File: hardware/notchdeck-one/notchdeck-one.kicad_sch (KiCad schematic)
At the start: 0 parts

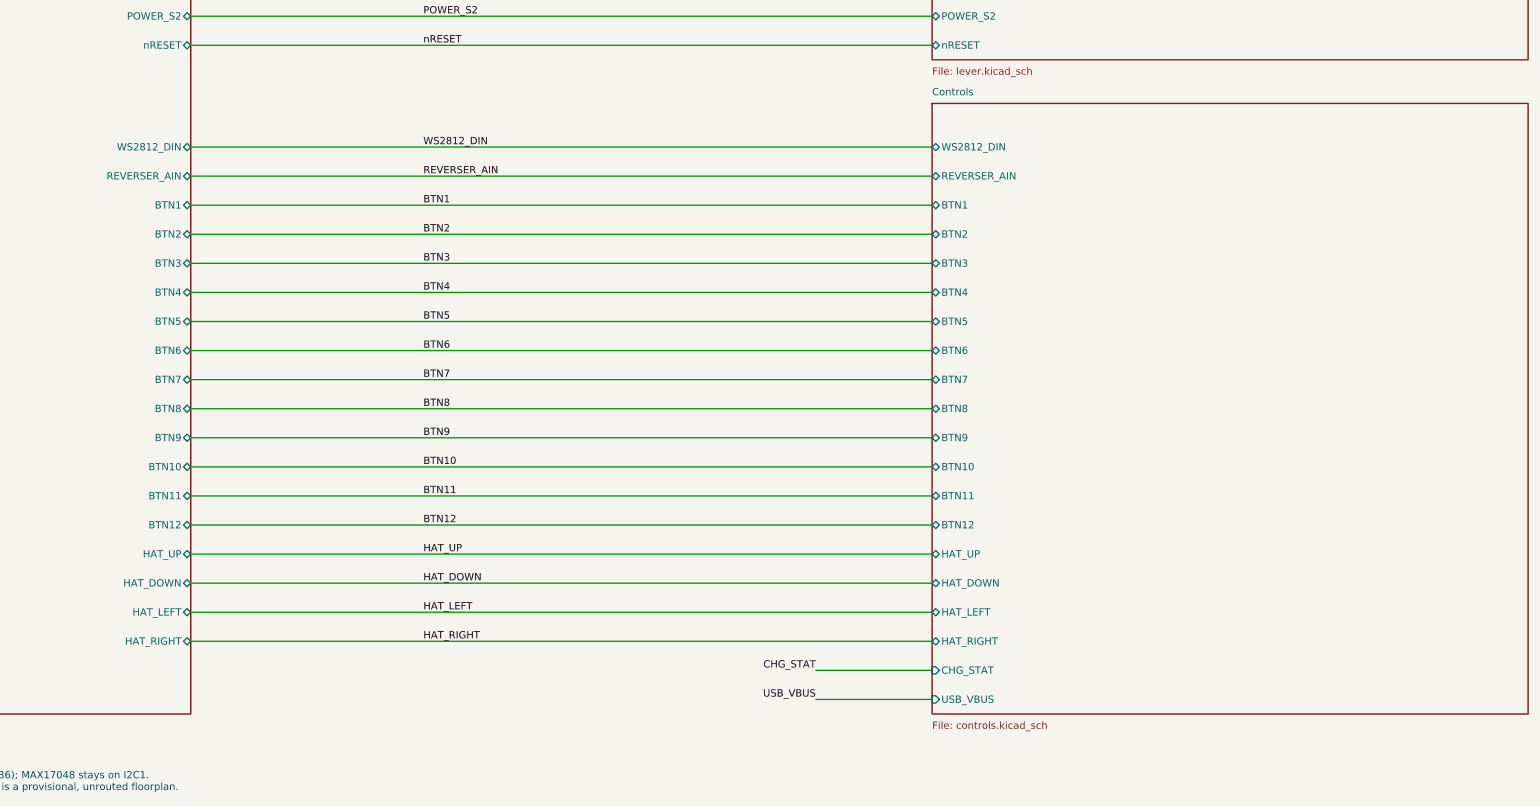
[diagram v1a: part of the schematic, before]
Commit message: Split controller buttons onto stocked STM32G030 panel PCB
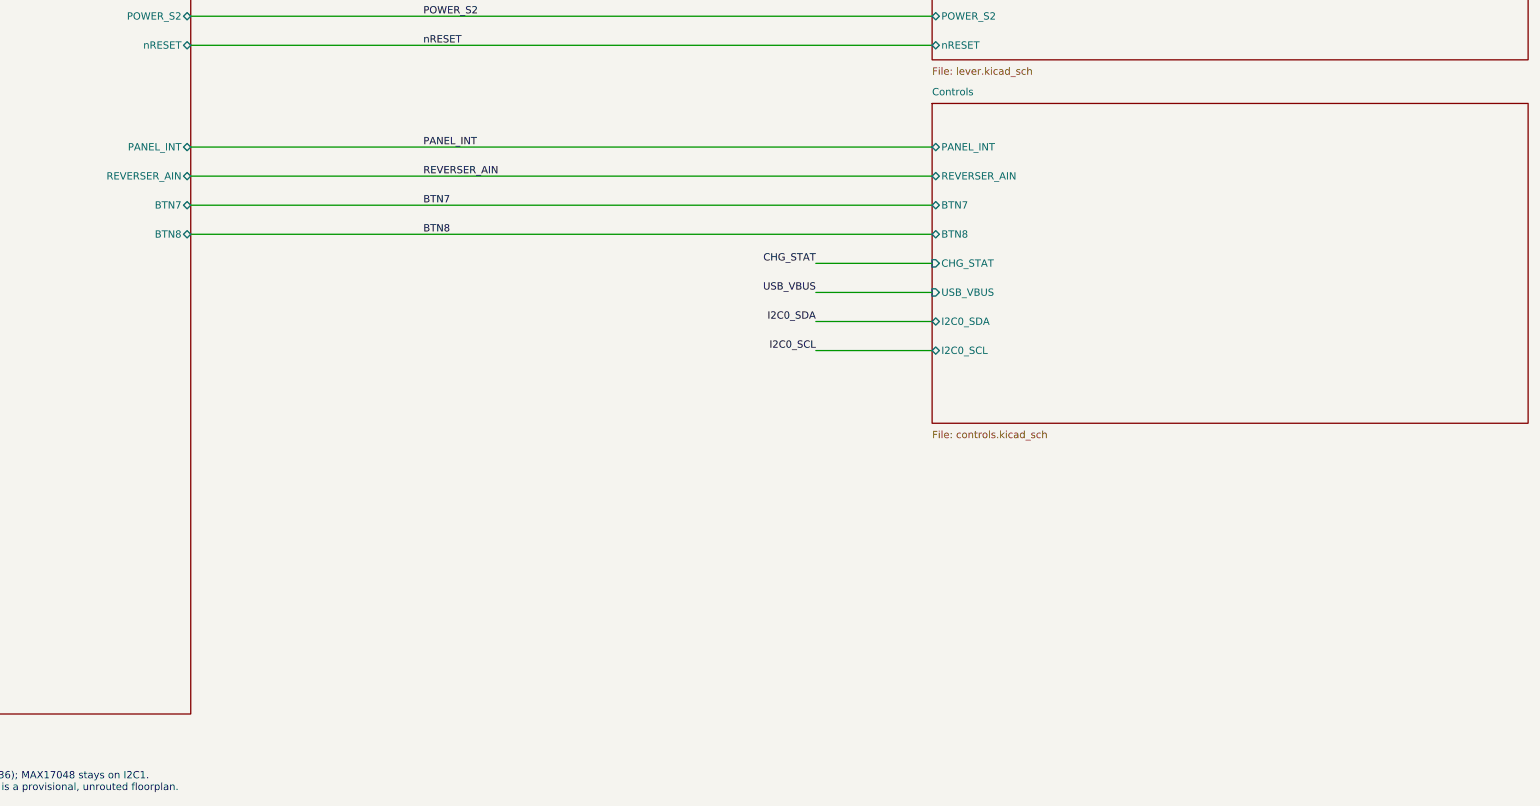
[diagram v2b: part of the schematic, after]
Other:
- sheet Controls ports: added I2C0_SCL, I2C0_SDA, PANEL_INT; removed BTN1, BTN10, BTN11, BTN12, BTN2, BTN3, BTN4, BTN5, BTN6, BTN9, HAT_DOWN, HAT_LEFT, HAT_RIGHT, HAT_UP, WS2812_DIN
- sheet MCU ports: added PANEL_INT; removed BTN1, BTN10, BTN11, BTN12, BTN2, BTN3, BTN4, BTN5, BTN6, BTN9, HAT_DOWN, HAT_LEFT, HAT_RIGHT, HAT_UP, WS2812_DIN
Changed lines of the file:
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@@
 		(title "NotchDeck One")
 		(date "2026-10-03")
-		(rev "D")
+		(rev "E")
 		(company "BenchBits")
 	)
@@
 	(sheet
 		(at 274.3200 147.3200)
-		(size 104.1400 106.6800)
+		(size 104.1400 55.8800)
 		(fields_autoplaced yes)
 		(stroke (width 0.1524) (type solid))
@@
 		)
 		(property "Sheetfile" "controls.kicad_sch"
-			(at 274.3200 255.2700 0)
+			(at 274.3200 204.4700 0)
 			(effects (font (size 1.27 1.27)) (justify left top))
 		)
-		(pin "WS2812_DIN" bidirectional
+		(pin "PANEL_INT" bidirectional
 			(at 274.3200 154.9400 180)
 			(effects (font (size 1.27 1.27)) (justify left))
@@
 			(effects (font (size 1.27 1.27)) (justify left))
 		)
-		(pin "BTN1" bidirectional
+		(pin "BTN7" bidirectional
 			(at 274.3200 165.1000 180)
 			(effects (font (size 1.27 1.27)) (justify left))
 		)
-		(pin "BTN2" bidirectional
+		(pin "BTN8" bidirectional
 			(at 274.3200 170.1800 180)
 			(effects (font (size 1.27 1.27)) (justify left))
 		)
-		(pin "BTN3" bidirectional
+		(pin "CHG_STAT" input
 			(at 274.3200 175.2600 180)
 			(effects (font (size 1.27 1.27)) (justify left))
 		)
-		(pin "BTN4" bidirectional
+		(pin "USB_VBUS" input
 			(at 274.3200 180.3400 180)
 			(effects (font (size 1.27 1.27)) (justify left))
 		)
-		(pin "BTN5" bidirectional
+		(pin "I2C0_SDA" bidirectional
 			(at 274.3200 185.4200 180)
 			(effects (font (size 1.27 1.27)) (justify left))
 		)
-		(pin "BTN6" bidirectional
+		(pin "I2C0_SCL" bidirectional
 			(at 274.3200 190.5000 180)
-			(effects (font (size 1.27 1.27)) (justify left))
-		)
-		(pin "BTN7" bidirectional
-			(at 274.3200 195.5800 180)
-			(effects (font (size 1.27 1.27)) (justify left))
-		)
-		(pin "BTN8" bidirectional
-			(at 274.3200 200.6600 180)
-			(effects (font (size 1.27 1.27)) (justify left))
-		)
-		(pin "BTN9" bidirectional
-			(at 274.3200 205.7400 180)
-			(effects (font (size 1.27 1.27)) (justify left))
-		)
-		(pin "BTN10" bidirectional
-			(at 274.3200 210.8200 180)
-			(effects (font (size 1.27 1.27)) (justify left))
-		)
-		(pin "BTN11" bidirectional
-			(at 274.3200 215.9000 180)
-			(effects (font (size 1.27 1.27)) (justify left))
-		)
-		(pin "BTN12" bidirectional
-			(at 274.3200 220.9800 180)
-			(effects (font (size 1.27 1.27)) (justify left))
-		)
-		(pin "HAT_UP" bidirectional
-			(at 274.3200 226.0600 180)
-			(effects (font (size 1.27 1.27)) (justify left))
-		)
-		(pin "HAT_DOWN" bidirectional
-			(at 274.3200 231.1400 180)
-			(effects (font (size 1.27 1.27)) (justify left))
-		)
-		(pin "HAT_LEFT" bidirectional
-			(at 274.3200 236.2200 180)
-			(effects (font (size 1.27 1.27)) (justify left))
-		)
-		(pin "HAT_RIGHT" bidirectional
-			(at 274.3200 241.3000 180)
-			(effects (font (size 1.27 1.27)) (justify left))
-		)
-		(pin "CHG_STAT" input
-			(at 274.3200 246.3800 180)
-			(effects (font (size 1.27 1.27)) (justify left))
-		)
-		(pin "USB_VBUS" input
-			(at 274.3200 251.4600 180)
 			(effects (font (size 1.27 1.27)) (justify left))
 		)
@@
 			(effects (font (size 1.27 1.27)) (justify right))
 		)
-		(pin "WS2812_DIN" bidirectional
+		(pin "PANEL_INT" bidirectional
 			(at 144.7800 154.9400 0)
 			(effects (font (size 1.27 1.27)) (justify right))
@@
 			(effects (font (size 1.27 1.27)) (justify right))
 		)
-		(pin "BTN1" bidirectional
+		(pin "BTN7" bidirectional
 			(at 144.7800 165.1000 0)
 			(effects (font (size 1.27 1.27)) (justify right))
 		)
-		(pin "BTN2" bidirectional
+		(pin "BTN8" bidirectional
 			(at 144.7800 170.1800 0)
-			(effects (font (size 1.27 1.27)) (justify right))
-		)
-		(pin "BTN3" bidirectional
-			(at 144.7800 175.2600 0)
-			(effects (font (size 1.27 1.27)) (justify right))
-		)
-		(pin "BTN4" bidirectional
-			(at 144.7800 180.3400 0)
-			(effects (font (size 1.27 1.27)) (justify right))
-		)
-		(pin "BTN5" bidirectional
-			(at 144.7800 185.4200 0)
-			(effects (font (size 1.27 1.27)) (justify right))
-		)
-		(pin "BTN6" bidirectional
-			(at 144.7800 190.5000 0)
-			(effects (font (size 1.27 1.27)) (justify right))
-		)
-		(pin "BTN7" bidirectional
-			(at 144.7800 195.5800 0)
-			(effects (font (size 1.27 1.27)) (justify right))
-		)
-		(pin "BTN8" bidirectional
-			(at 144.7800 200.6600 0)
-			(effects (font (size 1.27 1.27)) (justify right))
-		)
-		(pin "BTN9" bidirectional
-			(at 144.7800 205.7400 0)
-			(effects (font (size 1.27 1.27)) (justify right))
-		)
-		(pin "BTN10" bidirectional
-			(at 144.7800 210.8200 0)
-			(effects (font (size 1.27 1.27)) (justify right))
-		)
-		(pin "BTN11" bidirectional
-			(at 144.7800 215.9000 0)
-			(effects (font (size 1.27 1.27)) (justify right))
-		)
-		(pin "BTN12" bidirectional
-			(at 144.7800 220.9800 0)
-			(effects (font (size 1.27 1.27)) (justify right))
-		)
-		(pin "HAT_UP" bidirectional
-			(at 144.7800 226.0600 0)
-			(effects (font (size 1.27 1.27)) (justify right))
-		)
-		(pin "HAT_DOWN" bidirectional
-			(at 144.7800 231.1400 0)
-			(effects (font (size 1.27 1.27)) (justify right))
-		)
-		(pin "HAT_LEFT" bidirectional
-			(at 144.7800 236.2200 0)
-			(effects (font (size 1.27 1.27)) (justify right))
-		)
-		(pin "HAT_RIGHT" bidirectional
-			(at 144.7800 241.3000 0)
 			(effects (font (size 1.27 1.27)) (justify right))
 		)
@@
 		(stroke (width 0) (type default))
 	)
-	(label "WS2812_DIN"
+	(label "PANEL_INT"
 		(at 185.4200 154.9400 0)
 		(effects (font (size 1.27 1.27)) (justify left bottom))
@@
 		(stroke (width 0) (type default))
 	)
-	(label "BTN1"
+	(label "BTN7"
 		(at 185.4200 165.1000 0)
 		(effects (font (size 1.27 1.27)) (justify left bottom))
@@
 		(stroke (width 0) (type default))
 	)
-	(label "BTN2"
+	(label "BTN8"
 		(at 185.4200 170.1800 0)
 		(effects (font (size 1.27 1.27)) (justify left bottom))
 	)
-	(wire (pts (xy 144.7800 175.2600) (xy 274.3200 175.2600))
-		(stroke (width 0) (type default))
-	)
-	(label "BTN3"
-		(at 185.4200 175.2600 0)
-		(effects (font (size 1.27 1.27)) (justify left bottom))
-	)
-	(wire (pts (xy 144.7800 180.3400) (xy 274.3200 180.3400))
-		(stroke (width 0) (type default))
-	)
-	(label "BTN4"
-		(at 185.4200 180.3400 0)
-		(effects (font (size 1.27 1.27)) (justify left bottom))
-	)
-	(wire (pts (xy 144.7800 185.4200) (xy 274.3200 185.4200))
-		(stroke (width 0) (type default))
-	)
-	(label "BTN5"
-		(at 185.4200 185.4200 0)
-		(effects (font (size 1.27 1.27)) (justify left bottom))
-	)
-	(wire (pts (xy 144.7800 190.5000) (xy 274.3200 190.5000))
-		(stroke (width 0) (type default))
-	)
-	(label "BTN6"
-		(at 185.4200 190.5000 0)
-		(effects (font (size 1.27 1.27)) (justify left bottom))
-	)
-	(wire (pts (xy 144.7800 195.5800) (xy 274.3200 195.5800))
-		(stroke (width 0) (type default))
-	)
-	(label "BTN7"
-		(at 185.4200 195.5800 0)
-		(effects (font (size 1.27 1.27)) (justify left bottom))
-	)
-	(wire (pts (xy 144.7800 200.6600) (xy 274.3200 200.6600))
-		(stroke (width 0) (type default))
-	)
-	(label "BTN8"
-		(at 185.4200 200.6600 0)
-		(effects (font (size 1.27 1.27)) (justify left bottom))
-	)
-	(wire (pts (xy 144.7800 205.7400) (xy 274.3200 205.7400))
-		(stroke (width 0) (type default))
-	)
-	(label "BTN9"
-		(at 185.4200 205.7400 0)
-		(effects (font (size 1.27 1.27)) (justify left bottom))
-	)
-	(wire (pts (xy 144.7800 210.8200) (xy 274.3200 210.8200))
-		(stroke (width 0) (type default))
-	)
-	(label "BTN10"
-		(at 185.4200 210.8200 0)
-		(effects (font (size 1.27 1.27)) (justify left bottom))
-	)
-	(wire (pts (xy 144.7800 215.9000) (xy 274.3200 215.9000))
-		(stroke (width 0) (type default))
-	)
-	(label "BTN11"
-		(at 185.4200 215.9000 0)
-		(effects (font (size 1.27 1.27)) (justify left bottom))
-	)
-	(wire (pts (xy 144.7800 220.9800) (xy 274.3200 220.9800))
-		(stroke (width 0) (type default))
-	)
-	(label "BTN12"
-		(at 185.4200 220.9800 0)
-		(effects (font (size 1.27 1.27)) (justify left bottom))
-	)
-	(wire (pts (xy 144.7800 226.0600) (xy 274.3200 226.0600))
-		(stroke (width 0) (type default))
-	)
-	(label "HAT_UP"
-		(at 185.4200 226.0600 0)
-		(effects (font (size 1.27 1.27)) (justify left bottom))
-	)
-	(wire (pts (xy 144.7800 231.1400) (xy 274.3200 231.1400))
-		(stroke (width 0) (type default))
-	)
-	(label "HAT_DOWN"
-		(at 185.4200 231.1400 0)
-		(effects (font (size 1.27 1.27)) (justify left bottom))
-	)
-	(wire (pts (xy 144.7800 236.2200) (xy 274.3200 236.2200))
-		(stroke (width 0) (type default))
-	)
-	(label "HAT_LEFT"
-		(at 185.4200 236.2200 0)
-		(effects (font (size 1.27 1.27)) (justify left bottom))
-	)
-	(wire (pts (xy 144.7800 241.3000) (xy 274.3200 241.3000))
-		(stroke (width 0) (type default))
-	)
-	(label "HAT_RIGHT"
-		(at 185.4200 241.3000 0)
-		(effects (font (size 1.27 1.27)) (justify left bottom))
-	)
-	(wire (pts (xy 254.0000 246.3800) (xy 274.3200 246.3800))
+	(wire (pts (xy 254.0000 175.2600) (xy 274.3200 175.2600))
 		(stroke (width 0) (type default))
 	)
 	(label "CHG_STAT"
-		(at 254.0000 246.3800 180)
+		(at 254.0000 175.2600 180)
 		(effects (font (size 1.27 1.27)) (justify right bottom))
 	)
-	(wire (pts (xy 254.0000 251.4600) (xy 274.3200 251.4600))
+	(wire (pts (xy 254.0000 180.3400) (xy 274.3200 180.3400))
 		(stroke (width 0) (type default))
 	)
 	(label "USB_VBUS"
-		(at 254.0000 251.4600 180)
+		(at 254.0000 180.3400 180)
 		(effects (font (size 1.27 1.27)) (justify right bottom))
 	)
+	(wire (pts (xy 254.0000 185.4200) (xy 274.3200 185.4200))
+		(stroke (width 0) (type default))
+	)
+	(label "I2C0_SDA"
+		(at 254.0000 185.4200 180)
+		(effects (font (size 1.27 1.27)) (justify right bottom))
+	)
+	(wire (pts (xy 254.0000 190.5000) (xy 274.3200 190.5000))
+		(stroke (width 0) (type default))
+	)
+	(label "I2C0_SCL"
+		(at 254.0000 190.5000 180)
+		(effects (font (size 1.27 1.27)) (justify right bottom))
+	)
